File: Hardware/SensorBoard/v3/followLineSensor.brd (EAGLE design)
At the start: 111.4 x 30.5 mm, 26 parts

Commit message: Minor changes in SensorBoard v3
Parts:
- moved RIR5 4.00 mm to (97.8, 11.2)
- moved C2 3.50 mm to (98.9, 17.9)
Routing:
- net VBAT: track 114.5 -> 120.0 mm, vias 0 -> 1
- net N$3: track 7.49 -> 3.49 mm
- net GND: track 153.2 -> 153.4 mm, vias 0 -> 1
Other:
- outline, holes or cut-outs redrawn
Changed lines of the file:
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@@
 <board>
 <plain>
-<wire x1="-5.85" y1="0" x2="105.08" y2="0" width="0" layer="20"/>
+<wire x1="-6.35" y1="0" x2="105.08" y2="0" width="0" layer="20"/>
 <wire x1="105.08" y1="0" x2="105.08" y2="30.47" width="0" layer="20"/>
 <wire x1="105.08" y1="30.47" x2="-6.35" y2="30.47" width="0" layer="20"/>
-<wire x1="-6.35" y1="30.47" x2="-5.85" y2="0" width="0" layer="20"/>
+<wire x1="-6.35" y1="30.47" x2="-6.35" y2="0" width="0" layer="20"/>
 </plain>
 <attributes>
@@
 </autorouter>
 <elements>
-<element name="C2" library="rcl" package="C1206" value="1uF" x="98.94" y="21.41"/>
+<element name="C2" library="rcl" package="C1206" value="1uF" x="98.94" y="17.91"/>
 <element name="IR0" library="led" package="LED5MM" value="" x="1.39" y="5.08" rot="R270"/>
 <element name="IR1" library="led" package="LED5MM" value="" x="26.67" y="5.08" rot="R270"/>
@@
 <element name="RIR3" library="SparkFun-Passives" package="1206" value="270" x="57.15" y="15.24" rot="R90"/>
 <element name="RIR4" library="SparkFun-Passives" package="1206" value="270" x="72.39" y="15.24" rot="R90"/>
-<element name="RIR5" library="SparkFun-Passives" package="1206" value="270" x="97.79" y="15.24" rot="R90"/>
+<element name="RIR5" library="SparkFun-Passives" package="1206" value="270" x="97.79" y="11.24" rot="R90"/>
 <element name="RL0" library="SparkFun-Passives" package="1206" value="18K" x="8.77" y="15.24" rot="R90"/>
 <element name="RL1" library="SparkFun-Passives" package="1206" value="18K" x="34.29" y="15.24" rot="R90"/>
@@
 <contactref element="R1" pad="2"/>
 <contactref element="C2" pad="1"/>
-<wire x1="8.77" y1="16.64" x2="97.79" y2="16.64" width="0.8128" layer="1"/>
 <wire x1="8.77" y1="16.64" x2="1.39" y2="16.64" width="0.8128" layer="1"/>
 <wire x1="8.67" y1="24.65" x2="8.67" y2="16.74" width="0.8128" layer="1"/>
 <wire x1="8.67" y1="16.74" x2="8.77" y2="16.64" width="0.8128" layer="1"/>
 <contactref element="SV1" pad="6"/>
-<wire x1="97.79" y1="26.67" x2="97.79" y2="16.64" width="0.8128" layer="1"/>
-<wire x1="97.79" y1="16.64" x2="97.54" y2="21.41" width="0" layer="19" extent="1-1"/>
-<wire x1="90.17" y1="16.64" x2="97.79" y2="16.64" width="0" layer="19" extent="1-1"/>
-<wire x1="72.39" y1="16.64" x2="90.17" y2="16.64" width="0" layer="19" extent="1-1"/>
-<wire x1="64.77" y1="16.64" x2="72.39" y2="16.64" width="0" layer="19" extent="1-1"/>
-<wire x1="57.15" y1="16.64" x2="64.77" y2="16.64" width="0" layer="19" extent="1-1"/>
-<wire x1="49.53" y1="16.64" x2="57.15" y2="16.64" width="0" layer="19" extent="1-1"/>
-<wire x1="41.91" y1="16.64" x2="49.53" y2="16.64" width="0" layer="19" extent="1-1"/>
-<wire x1="34.29" y1="16.64" x2="41.91" y2="16.64" width="0" layer="19" extent="1-1"/>
-<wire x1="26.67" y1="16.64" x2="34.29" y2="16.64" width="0" layer="19" extent="1-1"/>
+<wire x1="90.17" y1="16.64" x2="26.67" y2="16.64" width="0.8128" layer="1"/>
+<wire x1="26.67" y1="16.64" x2="8.77" y2="16.64" width="0.8128" layer="1"/>
+<wire x1="90.17" y1="16.64" x2="91.79" y2="16.64" width="0.8128" layer="1"/>
+<wire x1="91.79" y1="16.64" x2="97.79" y2="12.64" width="0.8128" layer="1"/>
+<wire x1="97.79" y1="12.64" x2="97.54" y2="12.89" width="0.8128" layer="1"/>
+<wire x1="97.54" y1="12.89" x2="97.54" y2="17.91" width="0.8128" layer="1"/>
+<wire x1="34.29" y1="16.64" x2="26.67" y2="16.64" width="0" layer="19" extent="1-1"/>
+<wire x1="41.91" y1="16.64" x2="34.29" y2="16.64" width="0" layer="19" extent="1-1"/>
+<wire x1="49.53" y1="16.64" x2="41.91" y2="16.64" width="0" layer="19" extent="1-1"/>
+<wire x1="57.15" y1="16.64" x2="49.53" y2="16.64" width="0" layer="19" extent="1-1"/>
+<wire x1="64.77" y1="16.64" x2="57.15" y2="16.64" width="0" layer="19" extent="1-1"/>
+<wire x1="72.39" y1="16.64" x2="64.77" y2="16.64" width="0" layer="19" extent="1-1"/>
+<wire x1="97.54" y1="17.91" x2="97.54" y2="21.5" width="0.8128" layer="1"/>
+<wire x1="97.54" y1="21.5" x2="97.5" y2="21.5" width="0.8128" layer="1"/>
+<via x="97.5" y="21.5" extent="1-16" drill="0.6" shape="square"/>
+<wire x1="97.5" y1="21.5" x2="97.5" y2="26.38" width="0.8128" layer="16"/>
+<wire x1="97.5" y1="26.38" x2="97.79" y2="26.67" width="0.8128" layer="16"/>
 </signal>
 <signal name="GND">
@@
 <wire x1="1.2" y1="4" x2="1.39" y2="3.81" width="0.8128" layer="1"/>
 <contactref element="SV1" pad="7"/>
-<wire x1="100.33" y1="26.67" x2="100.33" y2="4.83" width="0.8128" layer="1"/>
-<wire x1="100.33" y1="4.83" x2="99.5" y2="4" width="0.8128" layer="1"/>
+<wire x1="100.34" y1="4.84" x2="99.5" y2="4" width="0.8128" layer="1"/>
 <wire x1="99.5" y1="4" x2="97.98" y2="4" width="0.8128" layer="1"/>
 <wire x1="97.98" y1="4" x2="97.79" y2="3.81" width="0.8128" layer="1"/>
-<wire x1="100.33" y1="26.67" x2="100.34" y2="21.41" width="0" layer="19" extent="1-1"/>
+<wire x1="100.34" y1="4.84" x2="100.34" y2="17.91" width="0.8128" layer="1"/>
 <wire x1="8.77" y1="3.81" x2="1.39" y2="3.81" width="0" layer="19" extent="1-1"/>
 <wire x1="64.77" y1="3.81" x2="72.39" y2="3.81" width="0" layer="19" extent="1-1"/>
@@
 <wire x1="41.91" y1="3.81" x2="34.29" y2="3.81" width="0" layer="19" extent="1-1"/>
 <wire x1="26.67" y1="3.81" x2="34.29" y2="3.81" width="0" layer="19" extent="1-1"/>
+<wire x1="100.34" y1="17.91" x2="100.5" y2="18.07" width="0.8128" layer="1"/>
+<wire x1="100.5" y1="18.07" x2="100.5" y2="21.5" width="0.8128" layer="1"/>
+<via x="100.5" y="21.5" extent="1-16" drill="0.6" shape="square"/>
+<wire x1="100.5" y1="21.5" x2="100.5" y2="26.67" width="0.8128" layer="16"/>
+<wire x1="100.5" y1="26.67" x2="100.33" y2="26.67" width="0.8128" layer="16"/>
 </signal>
 <signal name="N$17">
@@
 <contactref element="RIR5" pad="1"/>
 <contactref element="IR5" pad="A"/>
-<wire x1="97.79" y1="6.35" x2="97.79" y2="13.84" width="0.8128" layer="1"/>
+<wire x1="97.79" y1="6.35" x2="97.79" y2="9.84" width="0.8128" layer="1"/>
 </signal>
 </signals>

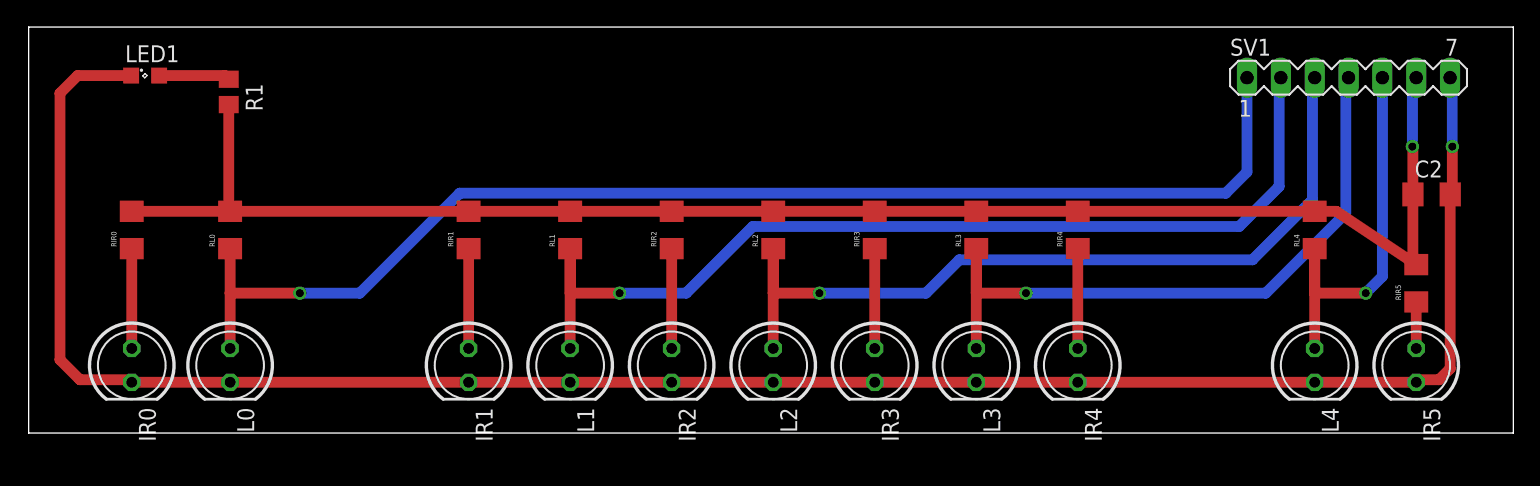
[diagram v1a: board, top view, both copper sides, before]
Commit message: Added copper pours to SensorBoard
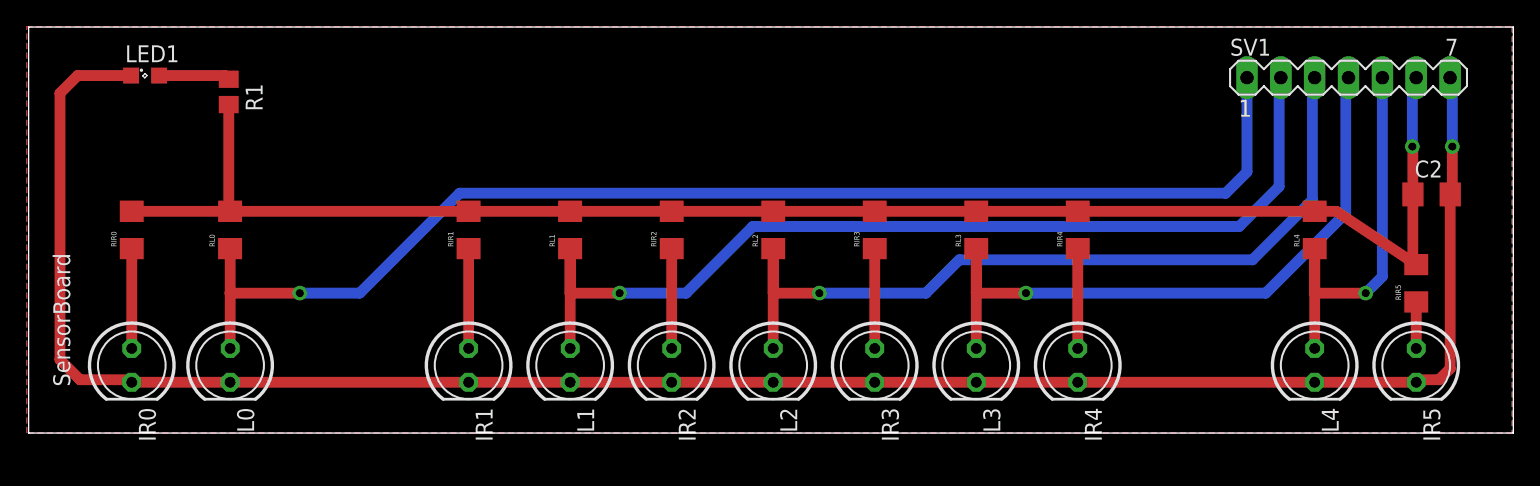
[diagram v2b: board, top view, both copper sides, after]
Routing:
- net GND: track 153.4 -> 161.3 mm
- added copper zone on layer 1, net GND
- added copper zone on layer 16, net GND
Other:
- board text added: "SensorBoard"
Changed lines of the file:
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@@
 <setting verticaltext="up"/>
 </settings>
-<grid distance="0.5" unitdist="mm" unit="mm" style="lines" multiple="1" display="yes" altdistance="0.025" altunitdist="inch" altunit="inch"/>
+<grid distance="0.5" unitdist="mm" unit="mm" style="lines" multiple="1" display="no" altdistance="0.025" altunitdist="inch" altunit="inch"/>
 <layers>
 <layer number="1" name="Top" color="4" fill="1" visible="yes" active="yes"/>
@@
 <wire x1="105.08" y1="30.47" x2="-6.35" y2="30.47" width="0" layer="20"/>
 <wire x1="-6.35" y1="30.47" x2="-6.35" y2="0" width="0" layer="20"/>
+<text x="-4.5" y="13.5" size="1.27" layer="21" rot="R270">SensorBoard</text>
 </plain>
 <attributes>
@@
 </class>
 </classes>
-<designrules name="default">
-<description language="de">&lt;b&gt;EAGLE Design Rules&lt;/b&gt;
-&lt;p&gt;
-Die Standard-Design-Rules sind so gewählt, dass sie für
-die meisten Anwendungen passen. Sollte ihre Platine
-besondere Anforderungen haben, treffen Sie die erforderlichen
-Einstellungen hier und speichern die Design Rules unter
-einem neuen Namen ab.</description>
+<designrules name="SparkFun">
 <description language="en">&lt;b&gt;EAGLE Design Rules&lt;/b&gt;
 &lt;p&gt;
@@
 <param name="mdViaViaSameLayer" value="8mil"/>
 <param name="mnLayersViaInSmd" value="2"/>
-<param name="mdCopperDimension" value="40mil"/>
+<param name="mdCopperDimension" value="8mil"/>
 <param name="mdDrill" value="8mil"/>
 <param name="mdSmdStop" value="0mil"/>
-<param name="msWidth" value="10mil"/>
-<param name="msDrill" value="24mil"/>
+<param name="msWidth" value="8mil"/>
+<param name="msDrill" value="20mil"/>
 <param name="msMicroVia" value="9.99mm"/>
 <param name="msBlindViaRatio" value="0.5"/>
@@
 <param name="rvMicroViaOuter" value="0.25"/>
 <param name="rvMicroViaInner" value="0.25"/>
-<param name="rlMinPadTop" value="10mil"/>
+<param name="rlMinPadTop" value="12mil"/>
 <param name="rlMaxPadTop" value="20mil"/>
 <param name="rlMinPadInner" value="10mil"/>
 <param name="rlMaxPadInner" value="20mil"/>
-<param name="rlMinPadBottom" value="10mil"/>
+<param name="rlMinPadBottom" value="12mil"/>
 <param name="rlMaxPadBottom" value="20mil"/>
-<param name="rlMinViaOuter" value="8mil"/>
+<param name="rlMinViaOuter" value="10mil"/>
 <param name="rlMaxViaOuter" value="20mil"/>
-<param name="rlMinViaInner" value="8mil"/>
+<param name="rlMinViaInner" value="10mil"/>
 <param name="rlMaxViaInner" value="20mil"/>
 <param name="rlMinMicroViaOuter" value="4mil"/>
@@
 <param name="mlMinCreamFrame" value="0mil"/>
 <param name="mlMaxCreamFrame" value="0mil"/>
-<param name="mlViaStopLimit" value="0mil"/>
+<param name="mlViaStopLimit" value="20mil"/>
 <param name="srRoundness" value="0"/>
 <param name="srMinRoundness" value="0mil"/>
@@
 <wire x1="8.67" y1="16.74" x2="8.77" y2="16.64" width="0.8128" layer="1"/>
 <contactref element="SV1" pad="6"/>
-<wire x1="90.17" y1="16.64" x2="26.67" y2="16.64" width="0.8128" layer="1"/>
+<wire x1="90.17" y1="16.64" x2="72.39" y2="16.64" width="0.8128" layer="1"/>
+<wire x1="72.39" y1="16.64" x2="64.77" y2="16.64" width="0.8128" layer="1"/>
+<wire x1="64.77" y1="16.64" x2="57.15" y2="16.64" width="0.8128" layer="1"/>
+<wire x1="57.15" y1="16.64" x2="49.53" y2="16.64" width="0.8128" layer="1"/>
+<wire x1="49.53" y1="16.64" x2="41.91" y2="16.64" width="0.8128" layer="1"/>
+<wire x1="41.91" y1="16.64" x2="34.29" y2="16.64" width="0.8128" layer="1"/>
+<wire x1="34.29" y1="16.64" x2="26.67" y2="16.64" width="0.8128" layer="1"/>
 <wire x1="26.67" y1="16.64" x2="8.77" y2="16.64" width="0.8128" layer="1"/>
 <wire x1="90.17" y1="16.64" x2="91.79" y2="16.64" width="0.8128" layer="1"/>
@@
 <wire x1="97.79" y1="12.64" x2="97.54" y2="12.89" width="0.8128" layer="1"/>
 <wire x1="97.54" y1="12.89" x2="97.54" y2="17.91" width="0.8128" layer="1"/>
-<wire x1="34.29" y1="16.64" x2="26.67" y2="16.64" width="0" layer="19" extent="1-1"/>
-<wire x1="41.91" y1="16.64" x2="34.29" y2="16.64" width="0" layer="19" extent="1-1"/>
-<wire x1="49.53" y1="16.64" x2="41.91" y2="16.64" width="0" layer="19" extent="1-1"/>
-<wire x1="57.15" y1="16.64" x2="49.53" y2="16.64" width="0" layer="19" extent="1-1"/>
-<wire x1="64.77" y1="16.64" x2="57.15" y2="16.64" width="0" layer="19" extent="1-1"/>
-<wire x1="72.39" y1="16.64" x2="64.77" y2="16.64" width="0" layer="19" extent="1-1"/>
 <wire x1="97.54" y1="17.91" x2="97.54" y2="21.5" width="0.8128" layer="1"/>
 <wire x1="97.54" y1="21.5" x2="97.5" y2="21.5" width="0.8128" layer="1"/>
@@
 <contactref element="LED1" pad="C"/>
 <contactref element="C2" pad="2"/>
-<wire x1="34.29" y1="3.81" x2="72.39" y2="3.81" width="0.8128" layer="1"/>
+<wire x1="34.29" y1="3.81" x2="41.91" y2="3.81" width="0.8128" layer="1"/>
+<wire x1="41.91" y1="3.81" x2="49.53" y2="3.81" width="0.8128" layer="1"/>
+<wire x1="49.53" y1="3.81" x2="57.15" y2="3.81" width="0.8128" layer="1"/>
+<wire x1="57.15" y1="3.81" x2="64.77" y2="3.81" width="0.8128" layer="1"/>
+<wire x1="64.77" y1="3.81" x2="72.39" y2="3.81" width="0.8128" layer="1"/>
 <wire x1="90.17" y1="3.81" x2="72.39" y2="3.81" width="0.8128" layer="1"/>
 <contactref element="IR5" pad="K"/>
 <wire x1="90.17" y1="3.81" x2="97.79" y2="3.81" width="0.8128" layer="1"/>
-<wire x1="34.29" y1="3.81" x2="1.39" y2="3.81" width="0.8128" layer="1"/>
+<wire x1="34.29" y1="3.81" x2="26.67" y2="3.81" width="0.8128" layer="1"/>
+<wire x1="26.67" y1="3.81" x2="8.77" y2="3.81" width="0.8128" layer="1"/>
+<wire x1="8.77" y1="3.81" x2="1.39" y2="3.81" width="0.8128" layer="1"/>
 <wire x1="1.34" y1="26.83" x2="-2.67" y2="26.83" width="0.8128" layer="1"/>
 <wire x1="-2.67" y1="26.83" x2="-4" y2="25.5" width="0.8128" layer="1"/>
@@
 <wire x1="97.98" y1="4" x2="97.79" y2="3.81" width="0.8128" layer="1"/>
 <wire x1="100.34" y1="4.84" x2="100.34" y2="17.91" width="0.8128" layer="1"/>
-<wire x1="8.77" y1="3.81" x2="1.39" y2="3.81" width="0" layer="19" extent="1-1"/>
-<wire x1="64.77" y1="3.81" x2="72.39" y2="3.81" width="0" layer="19" extent="1-1"/>
-<wire x1="57.15" y1="3.81" x2="64.77" y2="3.81" width="0" layer="19" extent="1-1"/>
-<wire x1="49.53" y1="3.81" x2="57.15" y2="3.81" width="0" layer="19" extent="1-1"/>
-<wire x1="41.91" y1="3.81" x2="34.29" y2="3.81" width="0" layer="19" extent="1-1"/>
-<wire x1="26.67" y1="3.81" x2="34.29" y2="3.81" width="0" layer="19" extent="1-1"/>
 <wire x1="100.34" y1="17.91" x2="100.5" y2="18.07" width="0.8128" layer="1"/>
 <wire x1="100.5" y1="18.07" x2="100.5" y2="21.5" width="0.8128" layer="1"/>
@@
 <wire x1="100.5" y1="21.5" x2="100.5" y2="26.67" width="0.8128" layer="16"/>
 <wire x1="100.5" y1="26.67" x2="100.33" y2="26.67" width="0.8128" layer="16"/>
+<wire x1="64.77" y1="3.81" x2="72.5" y2="3.81" width="0.4064" layer="1"/>
+<wire x1="72.5" y1="3.81" x2="72.5" y2="4" width="0.4064" layer="1"/>
+<polygon width="0.4064" layer="16" isolate="0.4064">
+<vertex x="-6.5" y="30.5"/>
+<vertex x="105" y="30.5"/>
+<vertex x="105" y="0"/>
+<vertex x="-6.5" y="0"/>
+</polygon>
+<polygon width="0.4064" layer="1" isolate="0.8128">
+<vertex x="-6.5" y="30.5"/>
+<vertex x="105" y="30.5"/>
+<vertex x="105" y="0"/>
+<vertex x="-6.5" y="0"/>
+</polygon>
 </signal>
 <signal name="N$17">
@@
 <wire x1="38" y1="10.5" x2="43" y2="10.5" width="0.8128" layer="16"/>
 <wire x1="43" y1="10.5" x2="48" y2="15.5" width="0.8128" layer="16"/>
-<wire x1="46" y1="13.5" x2="83.5" y2="13.5" width="0" layer="19" extent="1-16"/>
-<wire x1="83.5" y1="13.5" x2="87.5" y2="17.5" width="0" layer="19" extent="1-16"/>
 <wire x1="87.5" y1="26.54" x2="87.63" y2="26.67" width="0.8128" layer="16"/>
 <wire x1="87.5" y1="26.54" x2="87.5" y2="18.5" width="0.8128" layer="16"/>
 <wire x1="87.5" y1="18.5" x2="84.5" y2="15.5" width="0.8128" layer="16"/>
 <wire x1="84.5" y1="15.5" x2="48" y2="15.5" width="0.8128" layer="16"/>
-<wire x1="48" y1="15.5" x2="46" y2="13.5" width="0" layer="19" extent="1-16"/>
 </signal>
 <signal name="A2">
@@
 <via x="53" y="10.5" extent="1-16" drill="0.6" shape="square"/>
 <wire x1="53" y1="10.5" x2="61" y2="10.5" width="0.8128" layer="16"/>
-<wire x1="61" y1="10.5" x2="62.5" y2="12" width="0" layer="19" extent="1-16"/>
-<wire x1="62.5" y1="12" x2="85.5" y2="12" width="0" layer="19" extent="1-16"/>
-<wire x1="85.5" y1="12" x2="90" y2="16.5" width="0" layer="19" extent="1-16"/>
 <wire x1="90" y1="26.5" x2="90.17" y2="26.67" width="0.8128" layer="16"/>
 <wire x1="90" y1="26.5" x2="90" y2="17.5" width="0.8128" layer="16"/>

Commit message: Change led position
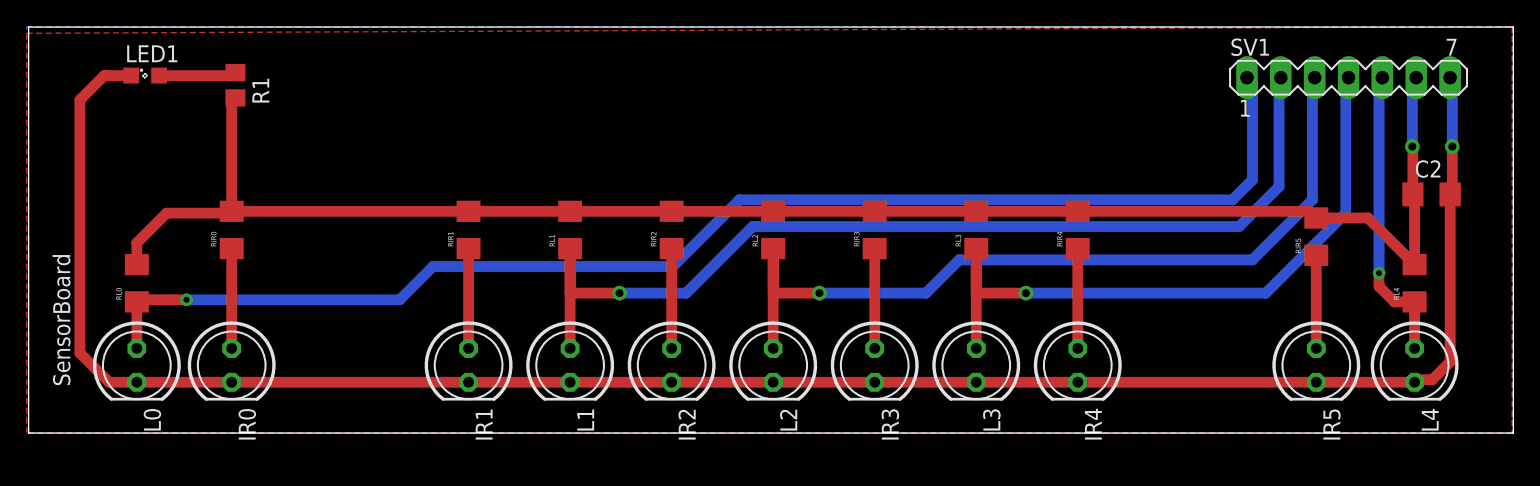
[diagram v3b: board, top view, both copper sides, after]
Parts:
- moved RL4 8.50 mm to (97.7, 11.2)
- moved RIR5 8.28 mm to (90.3, 14.7)
- moved RL0 8.06 mm to (1.77, 11.2)
- moved IR0 7.50 mm to (8.89, 5.08)
- moved RIR0 7.50 mm to (8.89, 15.2)
- moved IR5 7.50 mm to (90.3, 5.08)
- moved L4 7.50 mm to (97.7, 5.08)
- moved L0 7.00 mm to (1.77, 5.08)
- moved R1 0.71 mm to (9.17, 26.1)
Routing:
- net A4: track 31.3 -> 22.4 mm
- net A0: track 94.7 -> 98.9 mm
- net GND: track 161.3 -> 157.4 mm
- net N$3: track 3.49 -> 6.99 mm
- net VBAT: track 120.0 -> 123.0 mm
- added copper zone on layer 16, net N$4
- added copper zone on layer 1, net N$5
- removed copper zone on layer 1, net GND
- removed copper zone on layer 16, net GND
